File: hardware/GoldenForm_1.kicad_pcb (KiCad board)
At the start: 2 copper layers, 59 x 36.5 mm, 16 parts, among them IC1 UVLO, J1 SD_Socket, J2 USB_C_Receptacle_USB2.0_14P, J3 Conn_01x04_Pin, U1 Buck_Boost, U2 BNO055, U4 ESP32-S3-WROOM-1

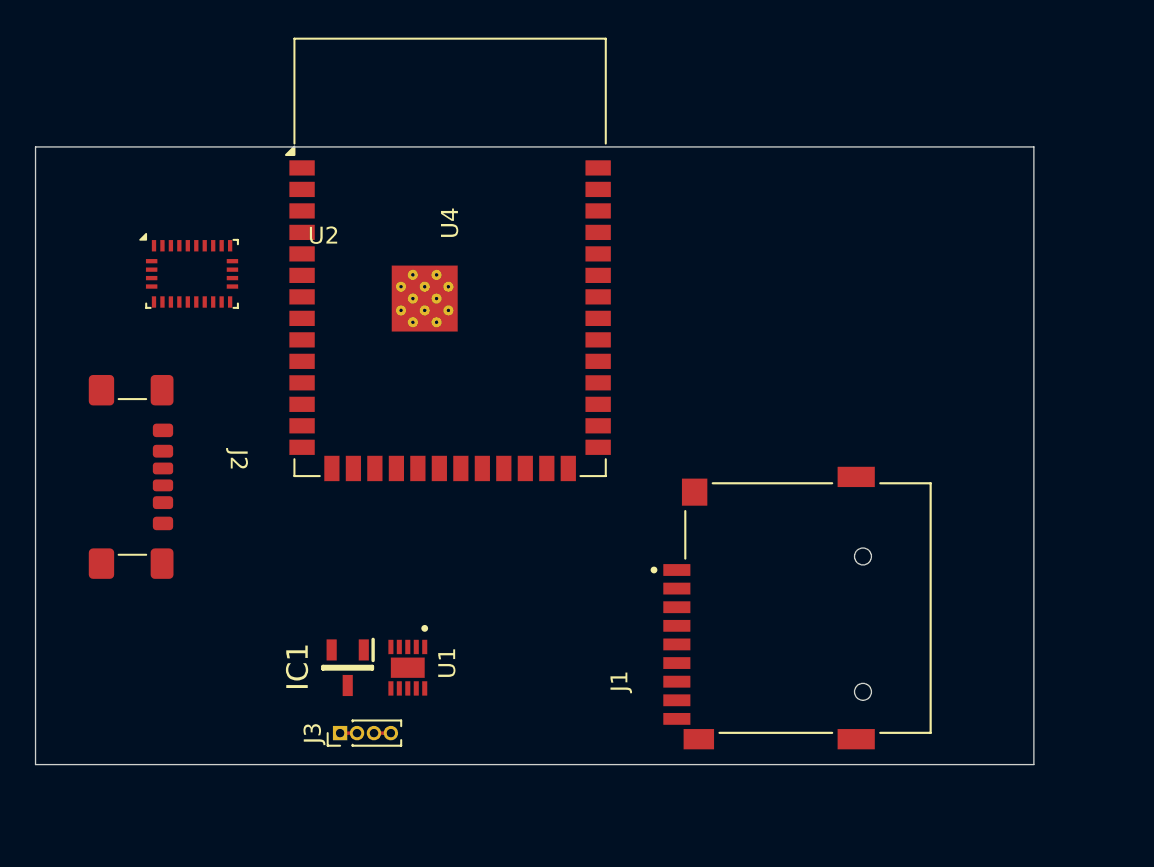
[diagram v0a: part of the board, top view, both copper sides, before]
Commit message: added m3 mounting holes
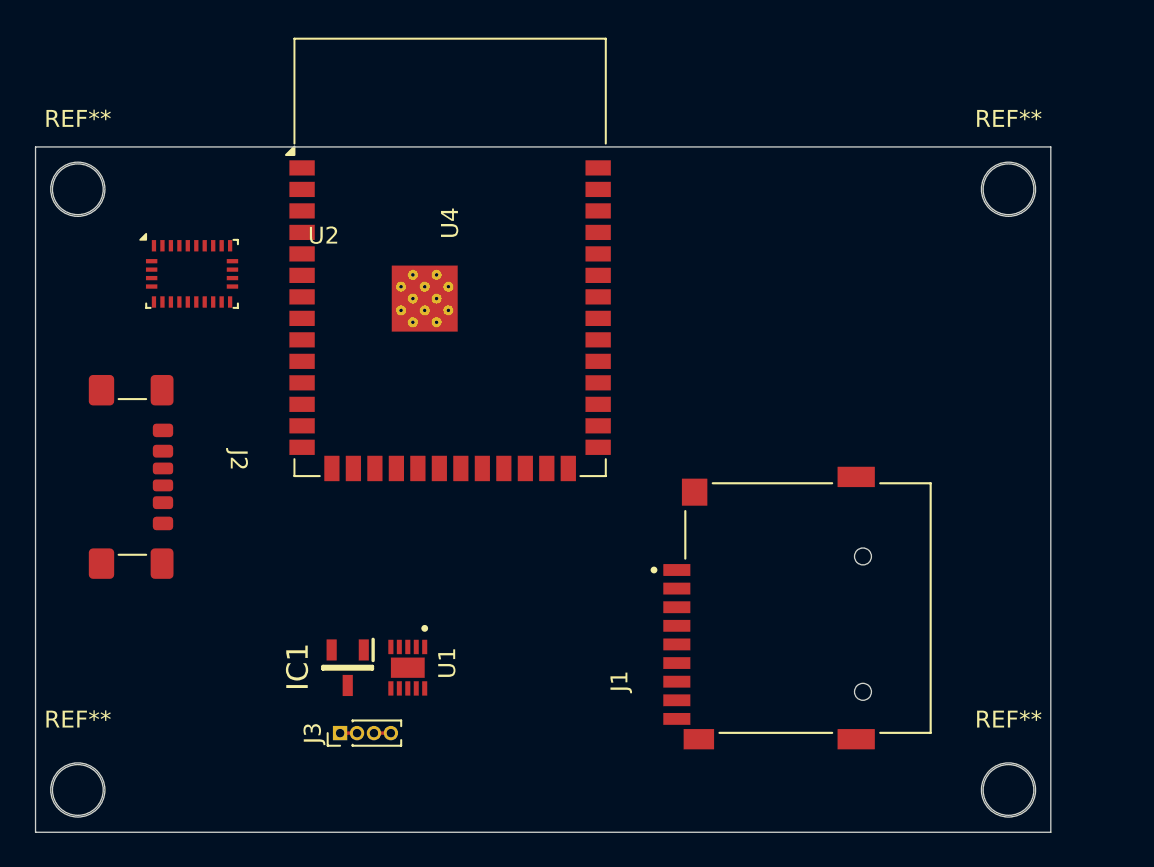
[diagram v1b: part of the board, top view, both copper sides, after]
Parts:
- added REF**: MountingHole_3.2mm_M3, MountingHole:MountingHole_3.2mm_M3, F.Cu at (70.0, 88.5)
- added REF**: MountingHole_3.2mm_M3, MountingHole:MountingHole_3.2mm_M3, F.Cu at (125.0, 88.5)
- added REF**: MountingHole_3.2mm_M3, MountingHole:MountingHole_3.2mm_M3, F.Cu at (70.0, 53.0)
- added REF**: MountingHole_3.2mm_M3, MountingHole:MountingHole_3.2mm_M3, F.Cu at (125.0, 53.0)
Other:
- board size 59 x 36.5 mm -> 60 x 40.5 mm

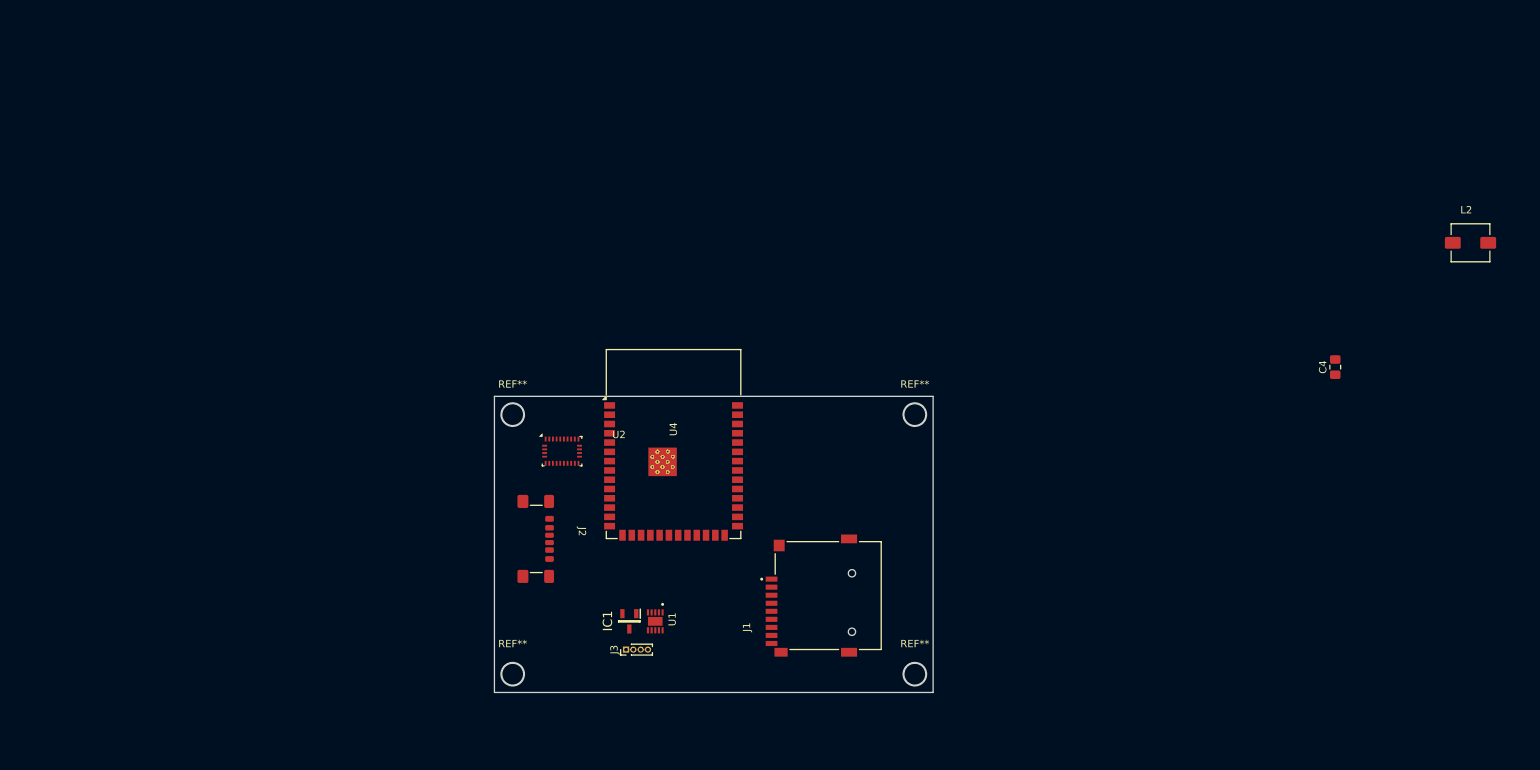
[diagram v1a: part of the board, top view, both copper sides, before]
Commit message: Fixing ERC Check Errors/Warnings (#22)
* some new changes

* more changes for ERC cleanup

* added Symbols to table

* wip

* WIP

* 3 ERC warnings now
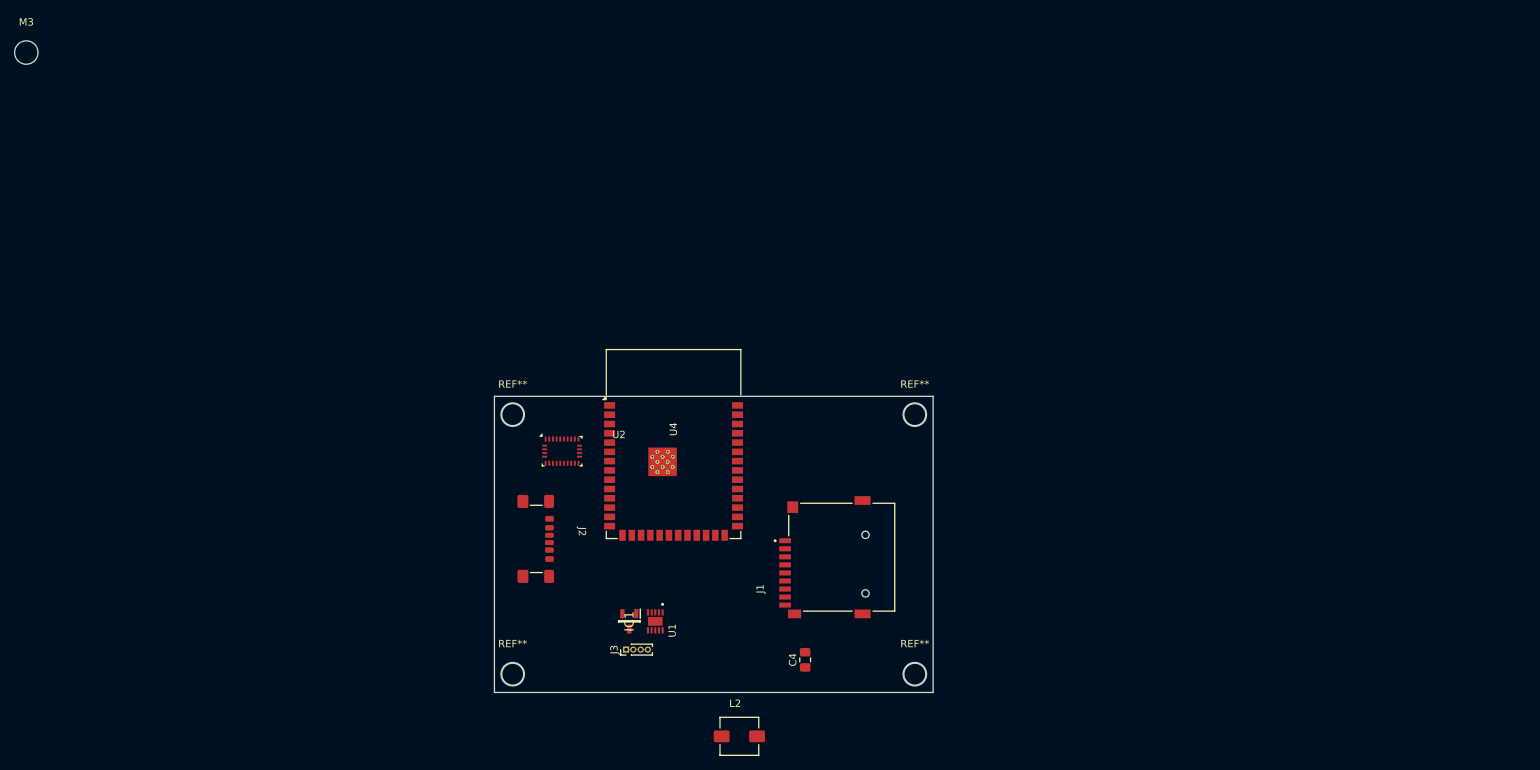
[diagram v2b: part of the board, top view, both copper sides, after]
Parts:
- added M3: MountingHole x 4, MountingHole:MountingHole_3.2mm_M3, F.Cu at (3.48, 3.48)
- IC1: footprint Library:SOT95P237X112-3N -> MyFootprints:SOT95P237X112-3N
- J1: footprint Library:CUI_MSD-4-A -> MyFootprints:CUI_MSD-4-A
- L2: footprint Library:INDM5752X300N -> MyFootprints:INDM5752X300N
- U1: footprint Library:SON50P250X250X80-11N -> MyFootprints:SON50P250X250X80-11N
- moved L2 120.6 mm to (101.0, 97.0)
- moved C4 82.8 mm to (110.0, 86.5)
- moved J1 5.57 mm to (115.0, 72.5)
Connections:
- C6 pad 1: GNDIO -> GND
- J1 pad CD: unconnected-(J1-PadCD) -> SD_DETECT
- J1 pad G1: unconnected-(J1-COVER_GND-PadG1) -> GND
- J1 pad G2: unconnected-(J1-COVER_GND__1-PadG2) -> GND
- J1 pad G3: unconnected-(J1-COVER_GND__2-PadG3) -> GND
- J1 pad G4: unconnected-(J1-COVER_GND__3-PadG4) -> GND
- U2 pad 18: GNDIO -> GND
- U2 pad 25: GNDIO -> GND
- U2 pad 4: unconnected-(U2-~{BOOT_LOAD_PIN}-Pad4) -> V_DD
- U2 pad 5: GNDIO -> GND
- U2 pad 6: GNDIO -> GND
- U4 pad 12: unconnected-(U4-IO8-Pad12) -> Net-(U4-IO8)
- U4 pad 17: unconnected-(U4-IO9-Pad17) -> Net-(U4-IO9)
- U4 pad 19: unconnected-(U4-IO11-Pad19) -> SD_DETECT
- U4 pad 31: unconnected-(U4-IO38-Pad31) -> HAPTIC
- U4 pad 38: unconnected-(U4-IO2-Pad38) -> Net-(U4-IO2)
- U4 pad 39: unconnected-(U4-IO1-Pad39) -> Net-(U4-IO1)
- U4 pad 4: unconnected-(U4-IO4-Pad4) -> SDA
- U4 pad 5: unconnected-(U4-IO5-Pad5) -> SCL
- U4 pad 6: unconnected-(U4-IO6-Pad6) -> I2C_ADDR
- U4 pad 7: unconnected-(U4-IO7-Pad7) -> INT

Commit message: some updates to footprints, USBC, buck boost, switch
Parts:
- removed J2: USB_C_Receptacle_USB2.0_14P, Connector_USB:USB_C_Receptacle_GCT_USB4135-GF-A_6P_TopMnt_Horizontal
- removed L2: SRP5030T-2R2M, MyFootprints:INDM5752X300N
- removed U1: Buck_Boost, MyFootprints:SON50P250X250X80-11N
- added J4: USB4105-GF-A, MyFootprints:USB4105_GCT, F.Cu at (72.3, 71.2)
- added S1: SLW-1276864-4A-D, MyFootprints:SLW12768644AD, F.Cu at (92.3, 82.8)
- added U3: Buck_Boost, MyFootprints:MICROSIP8_SIU_TEX, F.Cu at (86.5, 80.9)
- moved M3 66.8 mm to (58.2, 41.8)
- moved D1 9.13 mm to (230.0, 69.5)
- moved IC1 7.52 mm to (78.5, 82.3), turned to 90 degrees
- moved U4 2.25 mm to (94.2, 57.0)
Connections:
- net Net-(IC1-~{RESET}) renamed UVLO_EN

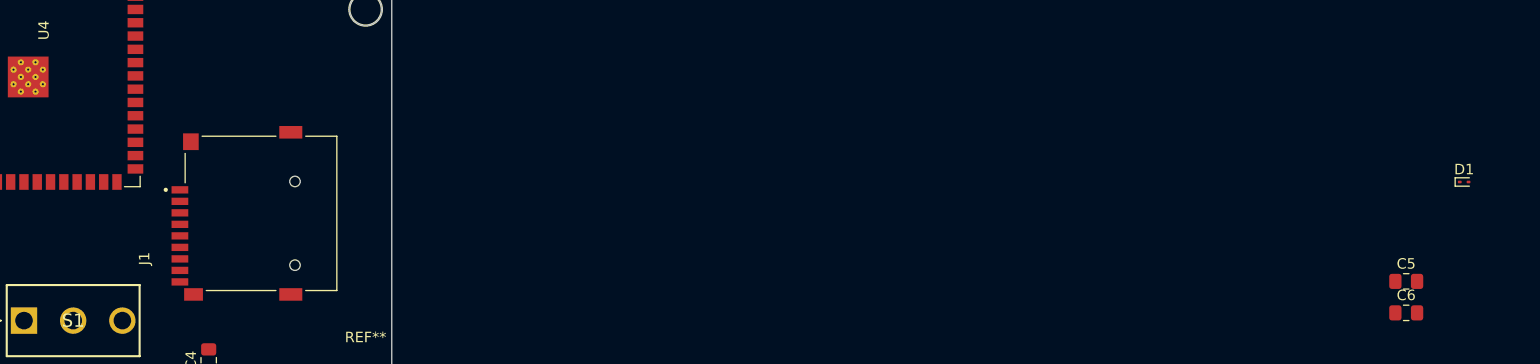
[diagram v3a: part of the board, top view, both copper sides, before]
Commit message: added new sd card socket, esd protection for boot and en, uart debug
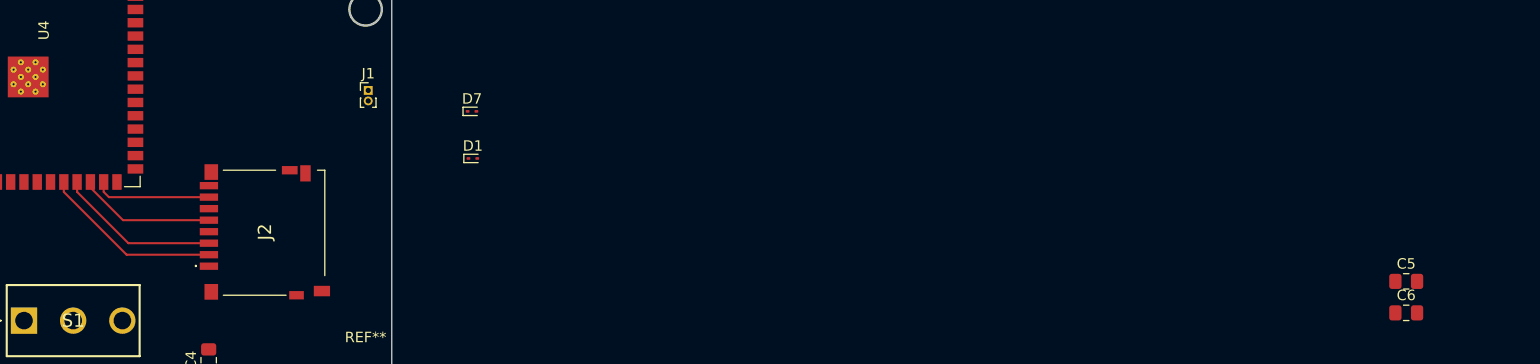
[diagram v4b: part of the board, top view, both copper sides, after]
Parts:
- added D7: ESD3.3, Diode_SMD:D_SOD-923, F.Cu at (135.2, 62.8)
- added J2: 1140084168, MyFootprints:1140084168, F.Cu at (115.4, 74.3)
- J1: value SD_Socket -> UART; footprint MyFootprints:CUI_MSD-4-A -> Connector_PinHeader_1.00mm:PinHeader_1x02_P1.00mm_Vertical
- J3: value Conn_01x04_Pin -> BATTERY
- moved D1 94.8 mm to (135.2, 67.2)
- moved J1 15.6 mm to (125.2, 60.8), turned to 0 degrees
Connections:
- D1 pad 2: Net-(D1-A2) -> BOOT_PIN
- J1 pad 1: unconnected-(J1-DAT2-Pad1) -> UART_TX
- J1 pad 2: CS -> UART_RX
- U4 pad 22: MISO -> CS
- U4 pad 23: SCK -> MOSI
- U4 pad 24: MOSI -> SCK
- U4 pad 25: CS -> MISO
- U4 pad 27: Net-(SW1-B) -> BOOT_PIN
- U4 pad 3: Net-(D1-A2) -> EN_PIN
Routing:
- net CS: track 0.00 -> 17.3 mm
- net MOSI: track 0.00 -> 15.6 mm
- net SCK: track 0.00 -> 13.2 mm
- net MISO: track 0.00 -> 11.2 mm

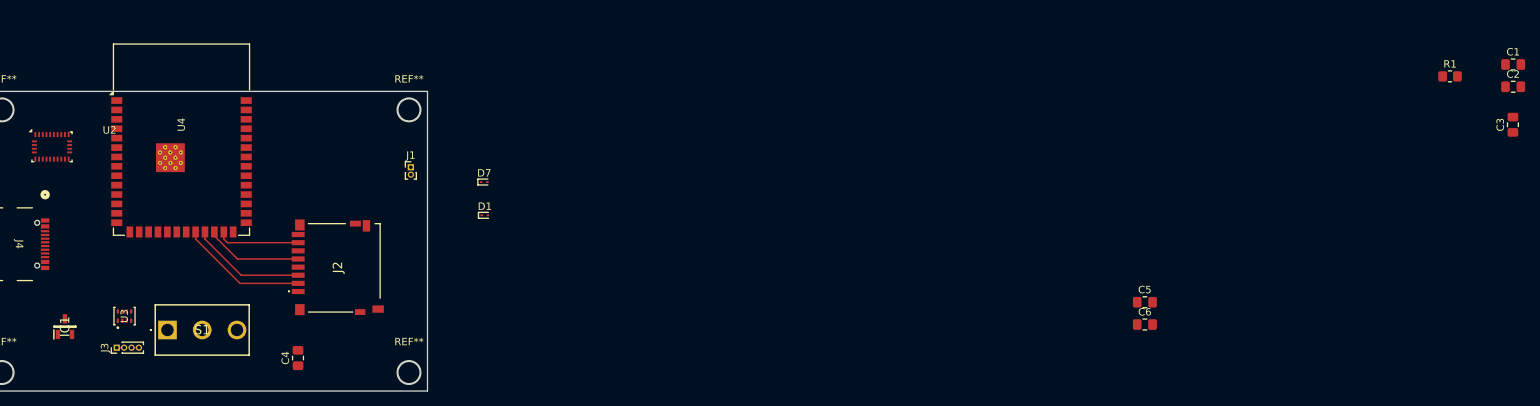
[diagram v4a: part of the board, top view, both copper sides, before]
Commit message: added switch, led footprints
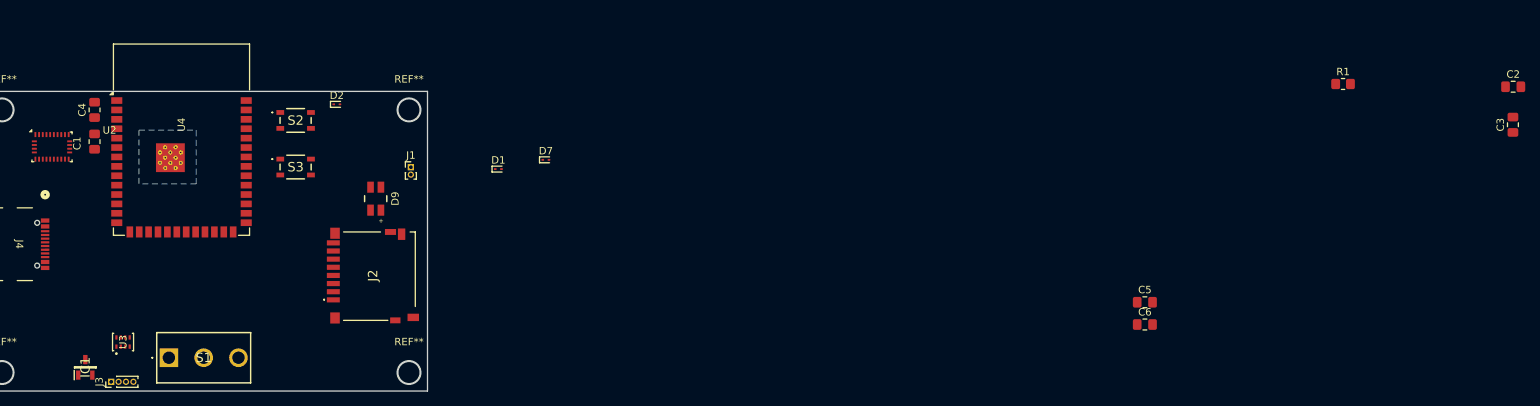
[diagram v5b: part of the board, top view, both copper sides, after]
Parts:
- added D2: ESD3.3, Diode_SMD:D_SOD-923, F.Cu at (115.2, 52.2)
- added D9: WL-SFTW_3528_PLCC4, MyFootprints:WL-SFTW_3528_PLCC4, F.Cu at (120.5, 65.0)
- added S2: PTS810SJM250SMTR_LFS, MyFootprints:PTS810SJM250SMTRLFS, F.Cu at (109.7, 54.4)
- added S3: PTS810SJM250SMTR_LFS, MyFootprints:PTS810SJM250SMTRLFS, F.Cu at (109.7, 60.7)
- J1: value UART -> Conn_01x02_Pin
- J3: value BATTERY -> Conn_01x04_Pin
- moved C1 192.0 mm to (82.5, 57.3), turned to 90 degrees
- moved C4 43.4 mm to (82.5, 53.0)
- moved R1 14.5 mm to (251.2, 49.5)
- moved D7 8.85 mm to (143.5, 59.8)
- moved D1 6.51 mm to (137.1, 61.0)
- moved IC1 6.15 mm to (81.2, 87.8)
- moved J2 4.88 mm to (120.1, 75.4)
- moved J3 4.67 mm to (84.8, 89.8)
- moved S1 3.76 mm to (92.5, 86.5)
- moved U3 3.51 mm to (86.3, 84.4)
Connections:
- U4 pad 12: Net-(U4-IO8) -> LOG_LED
- U4 pad 17: Net-(U4-IO9) -> SYNC_LED
- U4 pad 38: Net-(U4-IO2) -> LOG_LED
- U4 pad 39: Net-(U4-IO1) -> ERROR_LED
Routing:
- net CS: track 17.3 -> 0.00 mm
- net MOSI: track 15.6 -> 0.00 mm
- net SCK: track 13.2 -> 0.53 mm
- net MISO: track 11.2 -> 0.00 mm
- net D+: track 0.00 -> 1.06 mm
- net V_Bat: track 1.00 -> 0.00 mm
- net GND: track 1.00 -> 0.00 mm
- added copper zone on B.Cu, net GND
- added copper zone on In1.Cu, net GND
- added copper zone on In2.Cu, net V_DD
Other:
- copper layers 2 -> 4
